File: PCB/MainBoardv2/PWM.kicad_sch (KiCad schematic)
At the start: 11 parts, among them J10 Conn_01x03_Socket, J11 Conn_01x03_Socket, J12 Conn_01x03_Socket, J13 Conn_01x03_Socket, J14 Conn_01x04_Socket, J15 Conn_01x04_Socket, J16 Conn_01x04_Socket, J6 Conn_01x03_Socket, J8 Conn_01x03_Socket, J9 Conn_01x03_Socket

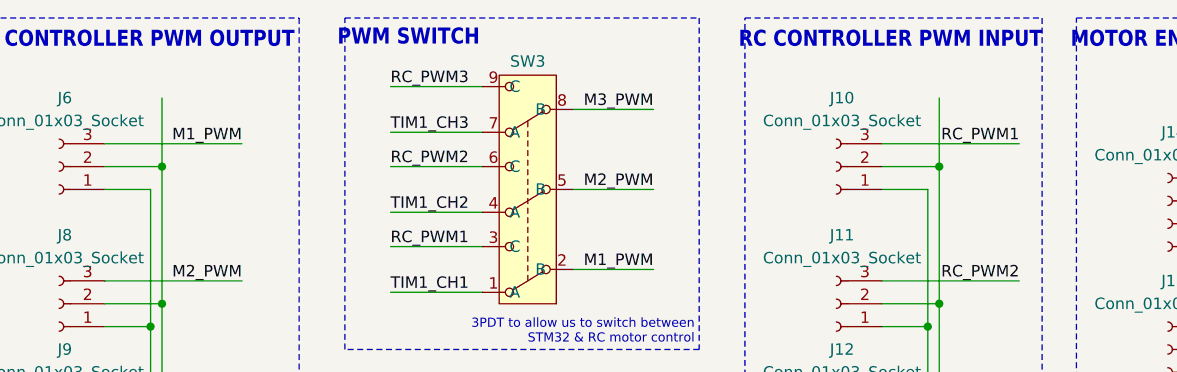
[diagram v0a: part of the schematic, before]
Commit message: updating main board v2 with motor power conns
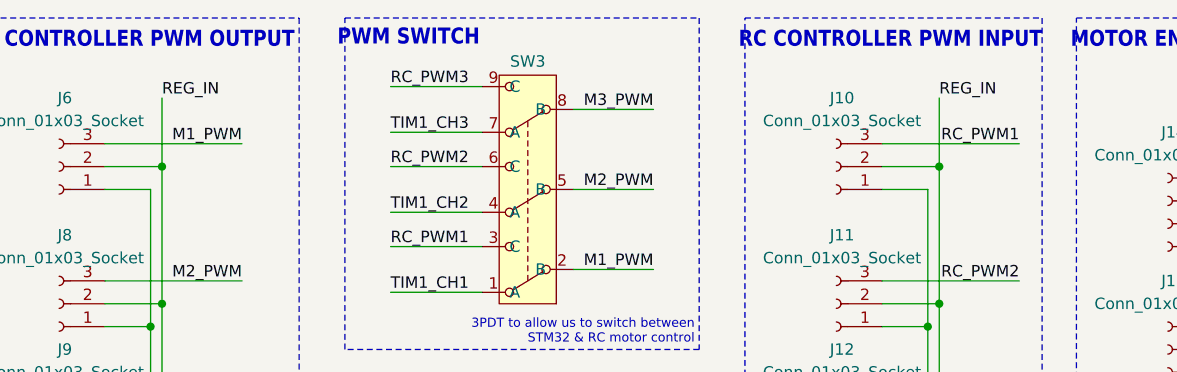
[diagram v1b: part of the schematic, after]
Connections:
- net REG_IN: now reaches J10.2 (Pin_2), J11.2 (Pin_2), J12.2 (Pin_2), J13.2 (Pin_2)
- net REG_IN: now also J6.2 (Pin_2), J8.2 (Pin_2), J9.2 (Pin_2)
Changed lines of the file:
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@@
+		)
+	)
+	(label "REG_IN"
+		(at 82.55 68.58 0)
+		(fields_autoplaced yes)
+		(effects
+			(font
+				(size 1.27 1.27)
+			)
+			(justify left bottom)
 		)
 	)
@@
 		(fields_autoplaced yes)
 		(effects
+			(font
+				(size 1.27 1.27)
+			)
+			(justify left bottom)
+		)
+	)
+	(label "REG_IN"
+		(at 168.91 68.58 0)
+		(fields_autoplaced yes)
+		(effects

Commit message: updating progress for board v2
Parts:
- added TP4, TP5, TP6: ~, TestPoint:TestPoint_Keystone_5000-5004_Miniature, symbol Connector:TestPoint
- J15: renamed from J14; footprint Connector_JST:JST_XH_B4B-XH-A_1x04_P2.50mm_Vertical -> Connector_JST:JST_PH_B4B-PH-K_1x04_P2.00mm_Vertical
- J18: renamed from J15; footprint Connector_JST:JST_XH_B4B-XH-A_1x04_P2.50mm_Vertical -> Connector_JST:JST_PH_B4B-PH-K_1x04_P2.00mm_Vertical
- J21: renamed from J16; footprint Connector_JST:JST_XH_B4B-XH-A_1x04_P2.50mm_Vertical -> Connector_JST:JST_PH_B4B-PH-K_1x04_P2.00mm_Vertical
- renumbered J6 to J13, J10 to J14, J8 to J16, J11 to J17, J9 to J19, J12 to J20, J13 to J22
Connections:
- net GND: no longer J22.3 (Pin_3)
- net M1_PWM: now also TP6.1
- net M2_PWM: now also TP5.1
- net M3_PWM: now also TP4.1
- net REG_IN: no longer J14.2 (Pin_2), J17.2 (Pin_2), J20.2 (Pin_2)
- no-connect marks 0 -> 4
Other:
- note added: "RC Receiver Power Input"

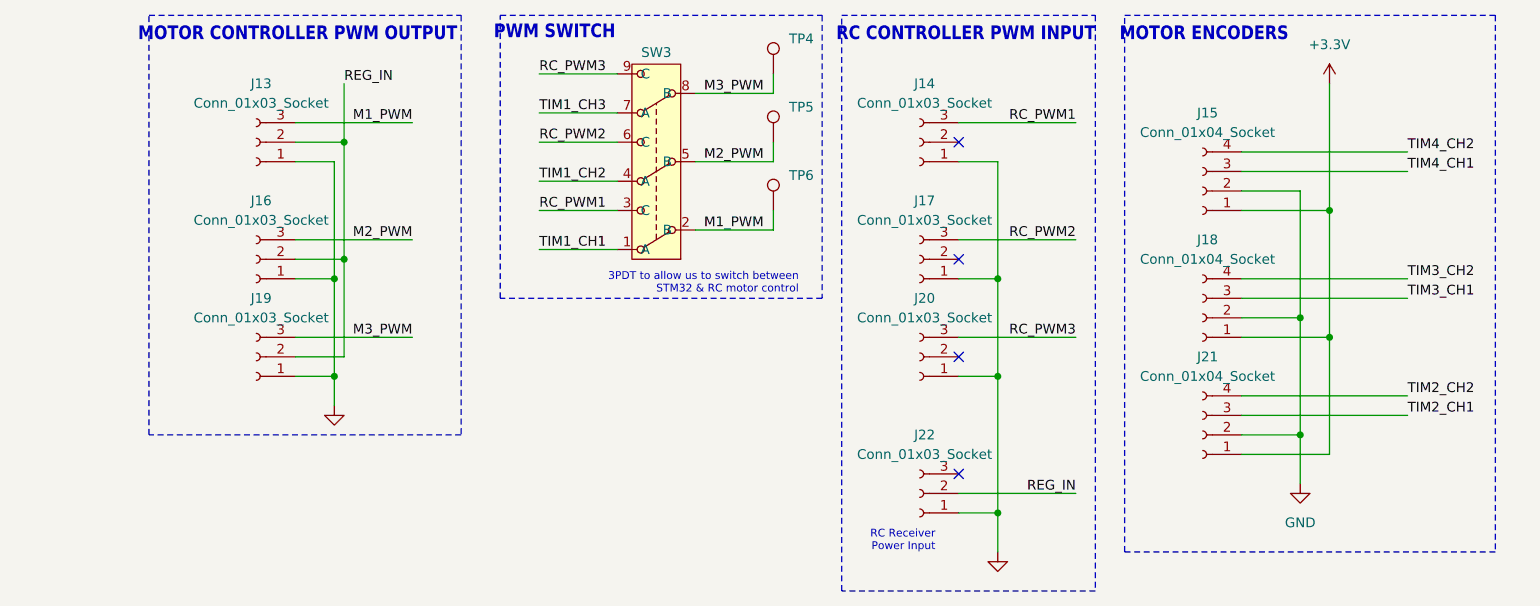
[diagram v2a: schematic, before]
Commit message: board v2 passing ERC in schematic
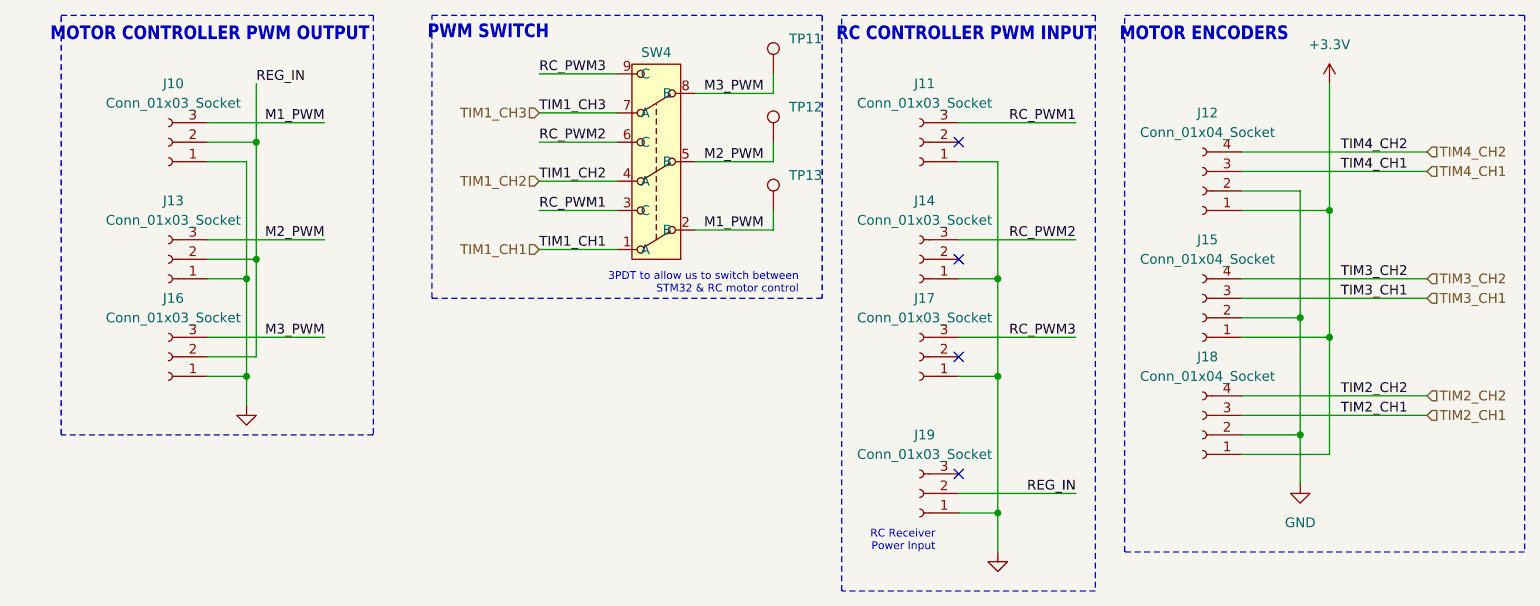
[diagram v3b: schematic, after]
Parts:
- renumbered J13 to J10, J14 to J11, J15 to J12, J16 to J13, J17 to J14, J18 to J15, J19 to J16, J20 to J17, J21 to J18, J22 to J19, SW3 to SW4, TP4 to TP11, TP5 to TP12, TP6 to TP13
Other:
- moved on the sheet: J10, J13, J16

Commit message: footprints all assigned for board v2
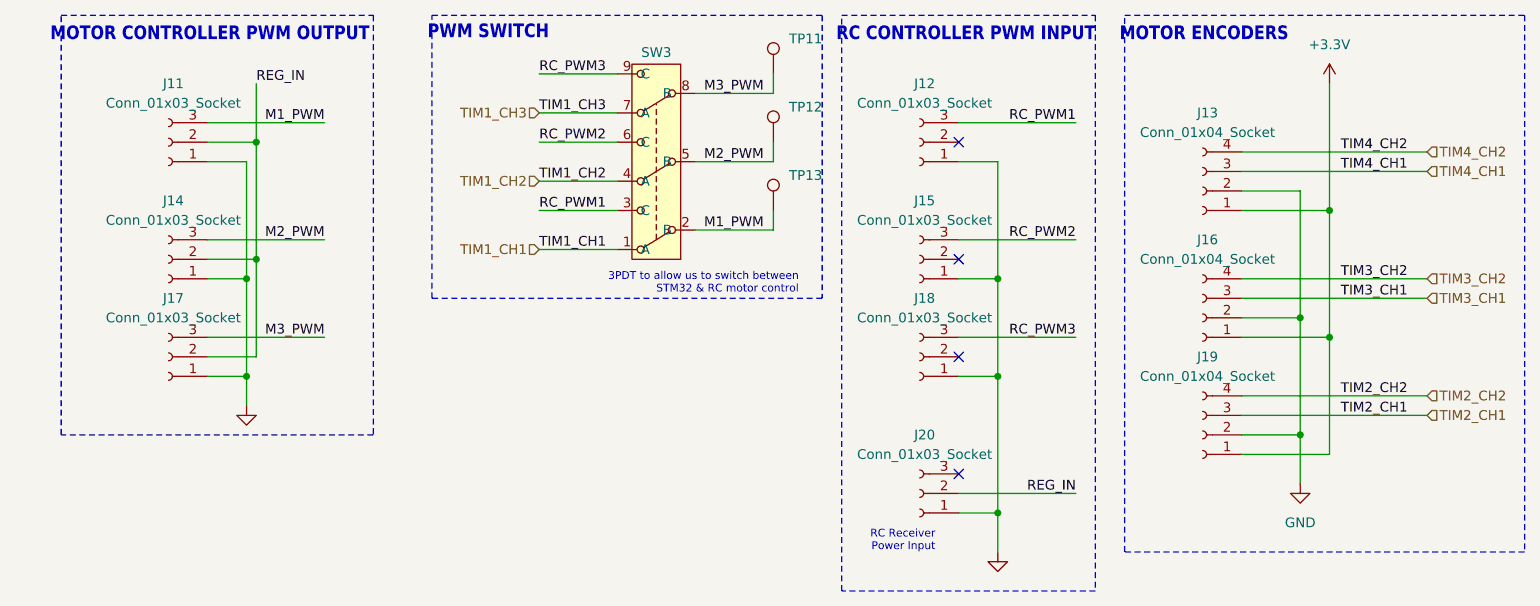
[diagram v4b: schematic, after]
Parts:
- renumbered J10 to J11, J11 to J12, J12 to J13, J13 to J14, J14 to J15, J15 to J16, J16 to J17, J17 to J18, J18 to J19, J19 to J20, SW4 to SW3
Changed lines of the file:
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@@
 		(dnp no)
 		(fields_autoplaced yes)
-		(property "Reference" "J18"
+		(property "Reference" "J19"
 			(at 194.945 104.14 0)
 			(effects
@@
 			(project "MainBoardv2"
 				(path "/d9c43b87-8960-41bd-bfcc-9c305bab2f72/cc711eab-7295-453b-97e2-e692aa39ee0f"
-					(reference "J18")
+					(reference "J19")
 					(unit 1)
 				)
@@
 		(dnp no)
 		(fields_autoplaced yes)
-		(property "Reference" "#PWR038"
+		(property "Reference" "#PWR042"
 			(at 167.64 135.89 0)
 			(effects
@@
 			(project "MainBoardv2"
 				(path "/d9c43b87-8960-41bd-bfcc-9c305bab2f72/cc711eab-7295-453b-97e2-e692aa39ee0f"
-					(reference "#PWR038")
+					(reference "#PWR042")
 					(unit 1)
 				)
@@
 		(on_board yes)
 		(dnp no)
-		(property "Reference" "J17"
+		(property "Reference" "J18"
 			(at 158.115 96.52 0)
 			(effects
@@
 			(project "MainBoardv2"
 				(path "/d9c43b87-8960-41bd-bfcc-9c305bab2f72/cc711eab-7295-453b-97e2-e692aa39ee0f"
-					(reference "J17")
+					(reference "J18")
 					(unit 1)
 				)
@@
 		(on_board yes)
 		(dnp no)
-		(property "Reference" "J16"
+		(property "Reference" "J17"
 			(at 60.325 96.52 0)
 			(effects
@@
 			(project "MainBoardv2"
 				(path "/d9c43b87-8960-41bd-bfcc-9c305bab2f72/cc711eab-7295-453b-97e2-e692aa39ee0f"
-					(reference "J16")
+					(reference "J17")
 					(unit 1)
 				)
@@
 		(on_board yes)
 		(dnp no)
-		(property "Reference" "SW4"
+		(property "Reference" "SW3"
 			(at 123.19 64.516 0)
 			(effects
@@
 			(project "MainBoardv2"
 				(path "/d9c43b87-8960-41bd-bfcc-9c305bab2f72/cc711eab-7295-453b-97e2-e692aa39ee0f"
-					(reference "SW4")
+					(reference "SW3")
 					(unit 1)
 				)
@@
 		(dnp no)
 		(fields_autoplaced yes)
-		(property "Reference" "#PWR037"
+		(property "Reference" "#PWR041"
 			(at 207.01 127 0)
 			(effects
@@
 			(project "MainBoardv2"
 				(path "/d9c43b87-8960-41bd-bfcc-9c305bab2f72/cc711eab-7295-453b-97e2-e692aa39ee0f"
-					(reference "#PWR037")
+					(reference "#PWR041")
 					(unit 1)
 				)
@@
 		(on_board yes)
 		(dnp no)
-		(property "Reference" "J11"
+		(property "Reference" "J12"
 			(at 158.115 68.58 0)
 			(effects
@@
 			(project "MainBoardv2"
 				(path "/d9c43b87-8960-41bd-bfcc-9c305bab2f72/cc711eab-7295-453b-97e2-e692aa39ee0f"
-					(reference "J11")
+					(reference "J12")
 					(unit 1)
 				)
@@
 		(dnp no)
 		(fields_autoplaced yes)
-		(property "Reference" "#PWR036"
+		(property "Reference" "#PWR040"
 			(at 69.85 116.84 0)
 			(effects
@@
 			(project "MainBoardv2"
 				(path "/d9c43b87-8960-41bd-bfcc-9c305bab2f72/cc711eab-7295-453b-97e2-e692aa39ee0f"
-					(reference "#PWR036")
+					(reference "#PWR040")
 					(unit 1)
 				)
@@
 		(dnp no)
 		(fields_autoplaced yes)
-		(property "Reference" "J12"
+		(property "Reference" "J13"
 			(at 194.945 72.39 0)
 			(effects
@@
 			(project "MainBoardv2"
 				(path "/d9c43b87-8960-41bd-bfcc-9c305bab2f72/cc711eab-7295-453b-97e2-e692aa39ee0f"
-					(reference "J12")
+					(reference "J13")
 					(unit 1)
 				)
@@
 		(on_board yes)
 		(dnp no)
-		(property "Reference" "J19"
+		(property "Reference" "J20"
 			(at 158.115 114.3 0)
 			(effects
@@
 			(project "MainBoardv2"
 				(path "/d9c43b87-8960-41bd-bfcc-9c305bab2f72/cc711eab-7295-453b-97e2-e692aa39ee0f"
-					(reference "J19")
+					(reference "J20")
 					(unit 1)
 				)
@@
 		(on_board yes)
 		(dnp no)
-		(property "Reference" "J14"
+		(property "Reference" "J15"
 			(at 158.115 83.82 0)
 			(effects
@@
 			(project "MainBoardv2"
 				(path "/d9c43b87-8960-41bd-bfcc-9c305bab2f72/cc711eab-7295-453b-97e2-e692aa39ee0f"
-					(reference "J14")
+					(reference "J15")
 					(unit 1)
 				)
@@
 		(dnp no)
 		(fields_autoplaced yes)
-		(property "Reference" "J15"
+		(property "Reference" "J16"
 			(at 194.945 88.9 0)
 			(effects
@@
 			(project "MainBoardv2"
 				(path "/d9c43b87-8960-41bd-bfcc-9c305bab2f72/cc711eab-7295-453b-97e2-e692aa39ee0f"
-					(reference "J15")
+					(reference "J16")
 					(unit 1)
 				)
@@
 		(on_board yes)
 		(dnp no)
-		(property "Reference" "J13"
+		(property "Reference" "J14"
 			(at 60.325 83.82 0)
 			(effects
@@
 			(project "MainBoardv2"
 				(path "/d9c43b87-8960-41bd-bfcc-9c305bab2f72/cc711eab-7295-453b-97e2-e692aa39ee0f"
-					(reference "J13")
+					(reference "J14")
 					(unit 1)
 				)
@@
 		(on_board yes)
 		(dnp no)
-		(property "Reference" "J10"
+		(property "Reference" "J11"
 			(at 60.325 68.58 0)
 			(effects
@@
 			(project "MainBoardv2"
 				(path "/d9c43b87-8960-41bd-bfcc-9c305bab2f72/cc711eab-7295-453b-97e2-e692aa39ee0f"
-					(reference "J10")
+					(reference "J11")
 					(unit 1)
 				)
@@
 		(dnp no)
 		(fields_autoplaced yes)
-		(property "Reference" "#PWR035"
+		(property "Reference" "#PWR039"
 			(at 210.82 72.39 0)
 			(effects
@@
 			(project "MainBoardv2"
 				(path "/d9c43b87-8960-41bd-bfcc-9c305bab2f72/cc711eab-7295-453b-97e2-e692aa39ee0f"
-					(reference "#PWR035")
-					(unit 1)
-				)
+					(reference "#PWR039")
+					(unit 1)
+				)

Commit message: Updated part assignments on board for digikey order
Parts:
- SW3: value ~ -> Slide
- TP11, TP12, TP13: value ~ -> White
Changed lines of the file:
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@@
 			)
 		)
-		(property "Datasheet" "~"
+		(property "Datasheet" "https://www.digikey.com/en/products/detail/jst-sales-america-inc./B4B-PH-K/768444?utm_adgroup=General&utm_source=google&utm_medium=cpc&utm_campaign=PMax%20Shopping_Product_Zombie%20SKUs&utm_term=&utm_content=General&utm_id=go_cmp-17815035045_adg-_ad-__dev-c_ext-_prd-768444_sig-Cj0KCQjw5cOwBhCiARIsAJ5njuaqARFbgUYS2KV_4JH144ujRm_jMbP6ua9XtI_O-O-_WbGcexelxyYaAqvOEALw_wcB&gad_source=1&gclid=Cj0KCQjw5cOwBhCiARIsAJ5njuaqARFbgUYS2KV_4JH144ujRm_jMbP6ua9XtI_O-O-_WbGcexelxyYaAqvOEALw_wcB"
 			(at 194.31 114.3 0)
 			(effects
@@
 			)
 		)
-		(property "Description" "Generic connector, single row, 01x04, script generated"
+		(property "Description" "Connector Header Through Hole 4 position 0.079\" (2.00mm)"
 			(at 194.31 114.3 0)
 			(effects
@@
 			)
 		)
-		(property "Value" "~"
+		(property "Value" "Slide"
 			(at 123.19 64.77 0)
 			(effects
@@
 					(size 1.27 1.27)
 				)
+				(hide yes)
 			)
 		)
@@
 			)
 		)
-		(property "Value" "~"
+		(property "Value" "White"
 			(at 140.462 74.168 0)
 			(effects
@@
 				)
 				(justify left)
+				(hide yes)
 			)
 		)
@@
 			)
 		)
-		(property "Datasheet" "~"
+		(property "Datasheet" "https://www.digikey.com/en/products/detail/keystone-electronics/5002/255328"
 			(at 143.51 76.2 0)
 			(effects
@@
 			)
 		)
-		(property "Description" ""
+		(property "Description" "White PC Test Point, Miniature Phosphor Bronze Silver Plating Through Hole Mounting Type"
 			(at 138.43 76.2 0)
 			(effects
@@
 			)
 		)
-		(property "Datasheet" "~"
+		(property "Datasheet" "https://www.digikey.com/en/products/detail/jst-sales-america-inc./B4B-PH-K/768444?utm_adgroup=General&utm_source=google&utm_medium=cpc&utm_campaign=PMax%20Shopping_Product_Zombie%20SKUs&utm_term=&utm_content=General&utm_id=go_cmp-17815035045_adg-_ad-__dev-c_ext-_prd-768444_sig-Cj0KCQjw5cOwBhCiARIsAJ5njuaqARFbgUYS2KV_4JH144ujRm_jMbP6ua9XtI_O-O-_WbGcexelxyYaAqvOEALw_wcB&gad_source=1&gclid=Cj0KCQjw5cOwBhCiARIsAJ5njuaqARFbgUYS2KV_4JH144ujRm_jMbP6ua9XtI_O-O-_WbGcexelxyYaAqvOEALw_wcB"
 			(at 194.31 82.55 0)
 			(effects
@@
 			)
 		)
-		(property "Description" "Generic connector, single row, 01x04, script generated"
+		(property "Description" "Connector Header Through Hole 4 position 0.079\" (2.00mm)"
 			(at 194.31 82.55 0)
 			(effects
@@
 			)
 		)
-		(property "Value" "~"
+		(property "Value" "White"
 			(at 140.462 65.278 0)
 			(effects
@@
 				)
 				(justify left)
+				(hide yes)
 			)
 		)
@@
 			)
 		)
-		(property "Datasheet" "~"
+		(property "Datasheet" "https://www.digikey.com/en/products/detail/keystone-electronics/5002/255328"
 			(at 143.51 67.31 0)
 			(effects
@@
 			)
 		)
-		(property "Description" ""
+		(property "Description" "White PC Test Point, Miniature Phosphor Bronze Silver Plating Through Hole Mounting Type"
 			(at 138.43 67.31 0)
 			(effects
@@
 			)
 		)
-		(property "Datasheet" "~"
+		(property "Datasheet" "https://www.digikey.com/en/products/detail/jst-sales-america-inc./B4B-PH-K/768444?utm_adgroup=General&utm_source=google&utm_medium=cpc&utm_campaign=PMax%20Shopping_Product_Zombie%20SKUs&utm_term=&utm_content=General&utm_id=go_cmp-17815035045_adg-_ad-__dev-c_ext-_prd-768444_sig-Cj0KCQjw5cOwBhCiARIsAJ5njuaqARFbgUYS2KV_4JH144ujRm_jMbP6ua9XtI_O-O-_WbGcexelxyYaAqvOEALw_wcB&gad_source=1&gclid=Cj0KCQjw5cOwBhCiARIsAJ5njuaqARFbgUYS2KV_4JH144ujRm_jMbP6ua9XtI_O-O-_WbGcexelxyYaAqvOEALw_wcB"
 			(at 194.31 99.06 0)
 			(effects
@@
 			)
 		)
-		(property "Description" "Generic connector, single row, 01x04, script generated"
+		(property "Description" "Connector Header Through Hole 4 position 0.079\" (2.00mm)"
 			(at 194.31 99.06 0)
 			(effects
@@
 			)
 		)
-		(property "Value" "~"
+		(property "Value" "White"
 			(at 140.462 83.058 0)
 			(effects
@@
 				)
 				(justify left)
+				(hide yes)
 			)
 		)
@@
 			)
 		)
-		(property "Datasheet" "~"
+		(property "Datasheet" "https://www.digikey.com/en/products/detail/keystone-electronics/5002/255328"
 			(at 143.51 85.09 0)
 			(effects
@@
 			)
 		)
-		(property "Description" ""
+		(property "Description" "White PC Test Point, Miniature Phosphor Bronze Silver Plating Through Hole Mounting Type"
 			(at 138.43 85.09 0)
 			(effects

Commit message: pushing progress on mainboard v2 layout
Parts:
- renumbered TP11 to TP12, TP12 to TP13, TP13 to TP14
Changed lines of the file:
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@@
 		(on_board yes)
 		(dnp no)
-		(property "Reference" "TP12"
+		(property "Reference" "TP13"
 			(at 140.462 71.628 0)
 			(effects
@@
 			(project "MainBoardv2"
 				(path "/d9c43b87-8960-41bd-bfcc-9c305bab2f72/cc711eab-7295-453b-97e2-e692aa39ee0f"
-					(reference "TP12")
+					(reference "TP13")
 					(unit 1)
 				)
@@
 		(on_board yes)
 		(dnp no)
-		(property "Reference" "TP11"
+		(property "Reference" "TP12"
 			(at 140.462 62.738 0)
 			(effects
@@
 			(project "MainBoardv2"
 				(path "/d9c43b87-8960-41bd-bfcc-9c305bab2f72/cc711eab-7295-453b-97e2-e692aa39ee0f"
-					(reference "TP11")
+					(reference "TP12")
 					(unit 1)
 				)
@@
 		(on_board yes)
 		(dnp no)
-		(property "Reference" "TP13"
+		(property "Reference" "TP14"
 			(at 140.462 80.518 0)
 			(effects
@@
 			(project "MainBoardv2"
 				(path "/d9c43b87-8960-41bd-bfcc-9c305bab2f72/cc711eab-7295-453b-97e2-e692aa39ee0f"
-					(reference "TP13")
-					(unit 1)
-				)
+					(reference "TP14")
+					(unit 1)
+				)
